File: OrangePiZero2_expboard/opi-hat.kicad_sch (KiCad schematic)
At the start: 37 parts, among them J1 Hydreon, J2 I2C, J3 SPI, J4 12Vin, J5 USB_C_Receptacle_USB2.0, J6 USB_B, J7 5Vout, U1 PC817, U2 LM2576-5.0, U3 LM1117-3.3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

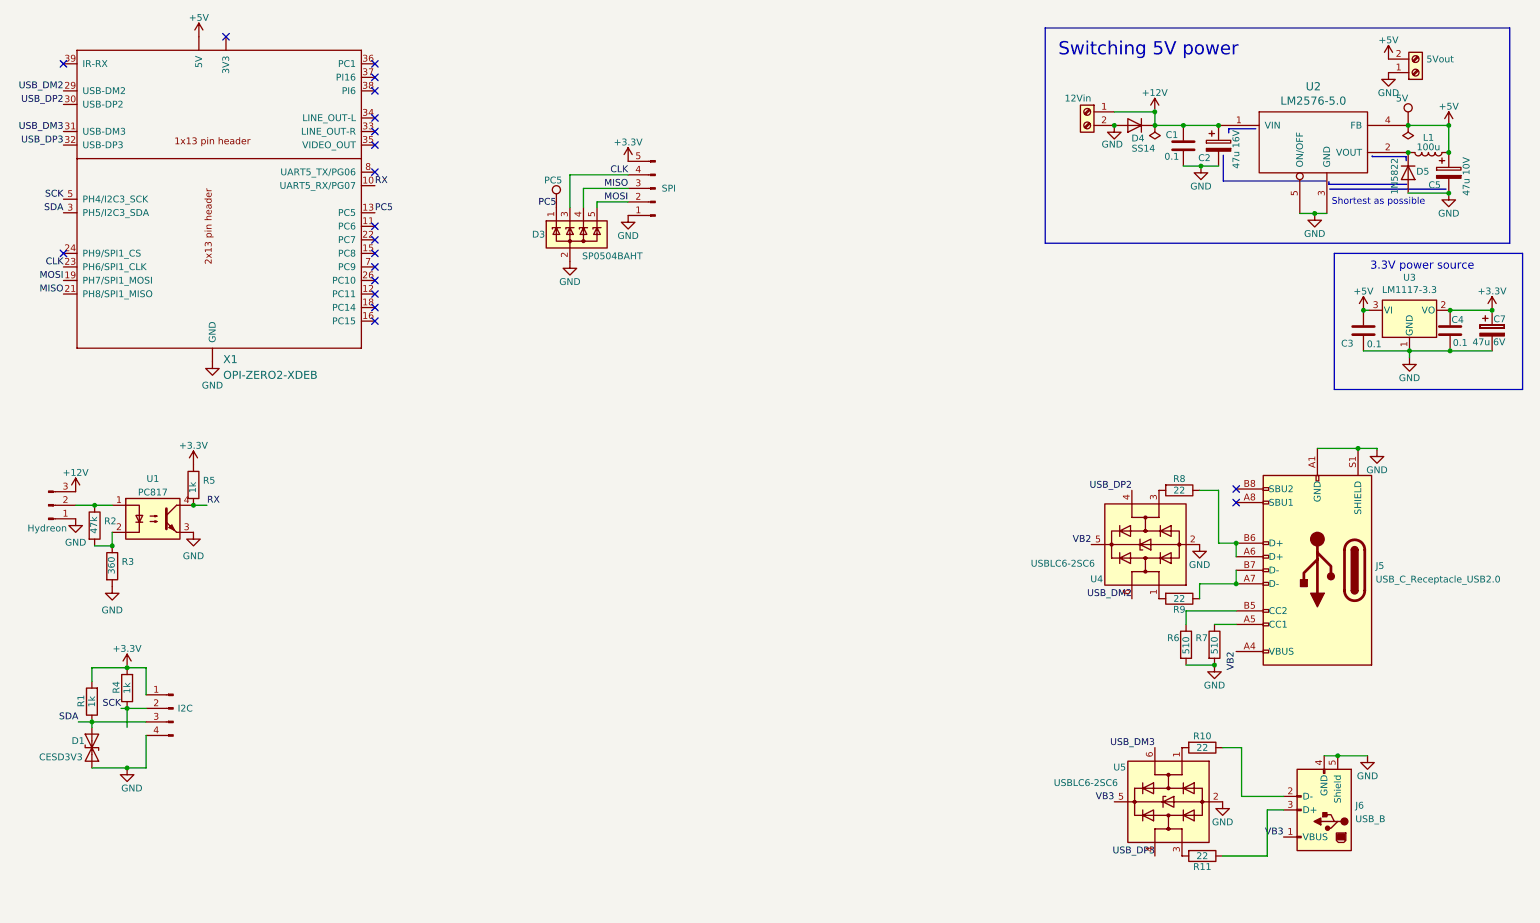
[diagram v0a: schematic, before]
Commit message: fixed boards on new kicad
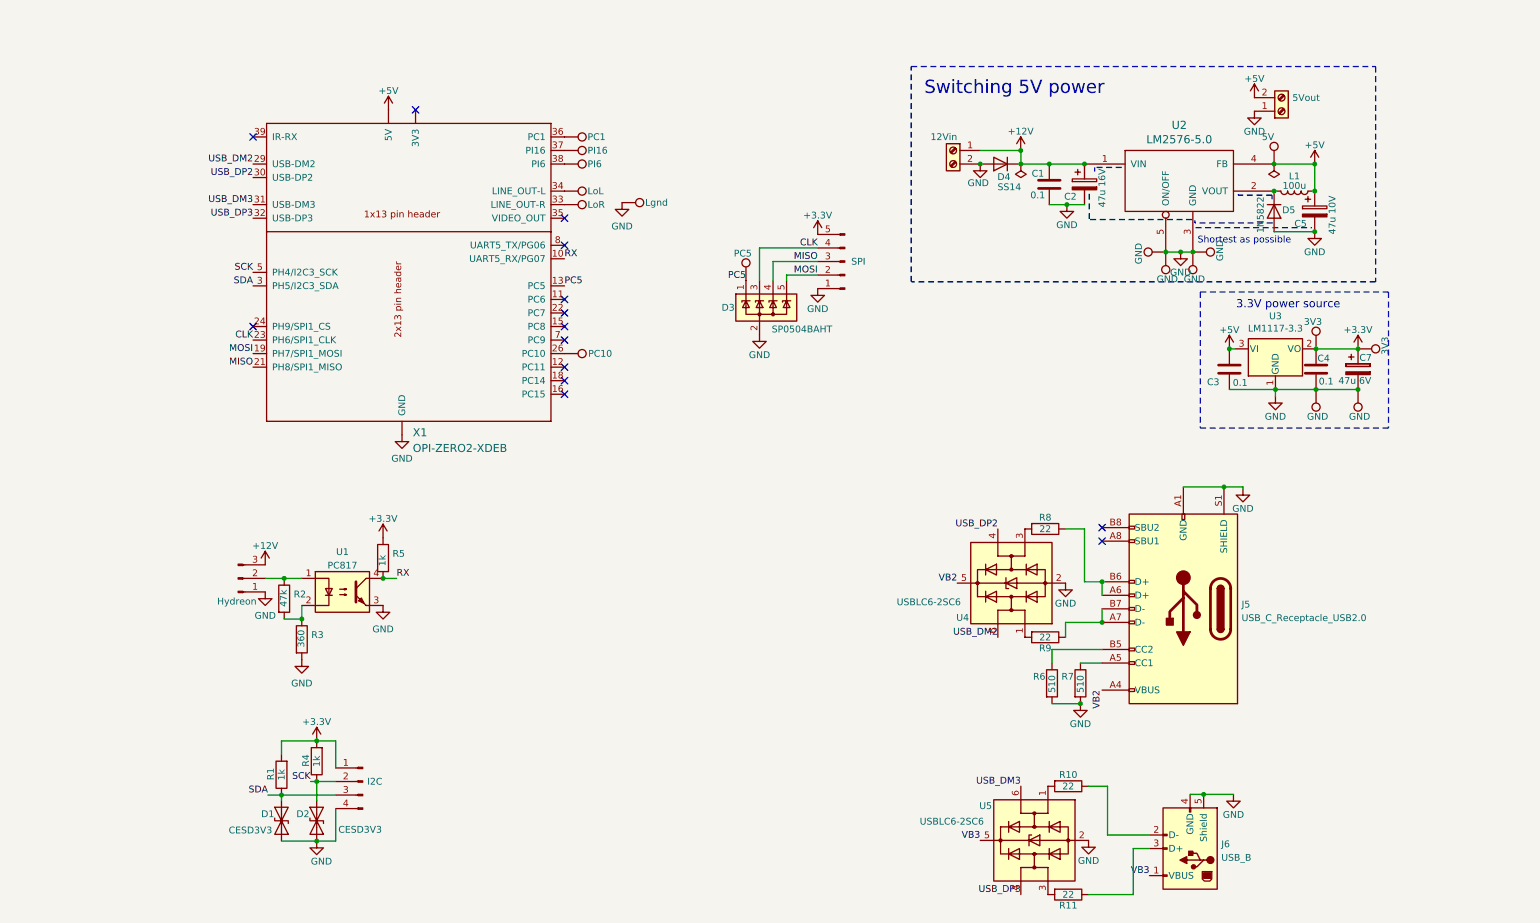
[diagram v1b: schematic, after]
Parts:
- added D2: CESD3V3, Diode_SMD:D_SOD-323_HandSoldering, symbol Diode:ESD9B3.3ST5G
- added TP1, TP13, TP14, TP15, TP17, TP2: GND, TestPoint:TestPoint_THTPad_2.5x2.5mm_Drill1.2mm, symbol Connector:TestPoint
- added TP10: LoL, TestPoint:TestPoint_THTPad_1.0x1.0mm_Drill0.5mm, symbol Connector:TestPoint
- added TP11: LoR, TestPoint:TestPoint_THTPad_1.0x1.0mm_Drill0.5mm, symbol Connector:TestPoint
- added TP12: Lgnd, TestPoint:TestPoint_THTPad_1.0x1.0mm_Drill0.5mm, symbol Connector:TestPoint
- added TP16, TP4: 3V3, TestPoint:TestPoint_THTPad_2.5x2.5mm_Drill1.2mm, symbol Connector:TestPoint
- added TP5: PC10, TestPoint:TestPoint_THTPad_2.5x2.5mm_Drill1.2mm, symbol Connector:TestPoint
- added TP6: PC1, TestPoint:TestPoint_THTPad_2.5x2.5mm_Drill1.2mm, symbol Connector:TestPoint
- added TP8: PI6, TestPoint:TestPoint_THTPad_2.5x2.5mm_Drill1.2mm, symbol Connector:TestPoint
- added TP9: PI16, TestPoint:TestPoint_THTPad_2.5x2.5mm_Drill1.2mm, symbol Connector:TestPoint
- gave numbers to parts that had none: 1
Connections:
- net +3.3V: now also TP16.1, TP4.1
- net GND: now also D2.2 (A2), TP1.1, TP12.1, TP13.1, TP14.1, TP15.1, TP17.1, TP2.1
- net SCK: now also D2.1 (A1)
- net at X1.26 (PC10): now also TP5.1
- net at X1.33 (LINE_OUT-R): now also TP11.1
- net at X1.34 (LINE_OUT-L): now also TP10.1
- net at X1.36 (PC1): now also TP6.1
- net at X1.37 (PI16): now also TP9.1
- net at X1.38 (PI6): now also TP8.1
- no-connect marks 20 -> 14
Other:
- moved on the sheet: C1, C2, C3, C4, C5, C7, D1, D3, D4, D5, J5, J6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
